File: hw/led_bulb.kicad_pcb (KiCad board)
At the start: 2 copper layers, 92.4 x 91.4 mm, 167 parts, among them P1 USB_OTG, P10 CONN_01X02, P11 CONN_01X02, P12 CONN_01X02, P13 CONN_01X02, P14 CONN_01X02, P15 CONN_01X02, P16 CONN_01X02, P17 CONN_01X02, P18 CONN_01X02, P19 CONN_01X02, P2 CONN_01X02, P20 CONN_01X02, P21 CONN_01X02, P22 CONN_01X02, P23 CONN_01X02, P24 CONN_01X02, P25 CONN_01X02, P26 CONN_01X02, P27 CONN_01X02, P28 CONN_01X02, P29 CONN_01X02, P3 CONN_01X02, P30 CONN_01X02, P31 CONN_01X02, P32 CONN_01X02, P33 CONN_01X02, P4 CONN_01X02, P5 CONN_01X02, P6 CONN_01X02, P7 CONN_01X02, P8 CONN_01X02, P9 CONN_01X02, SW1 SW_RST, SW2 SW_FLASH, U1 CP2102, U3 ESP-12E, U4 AP1117D33

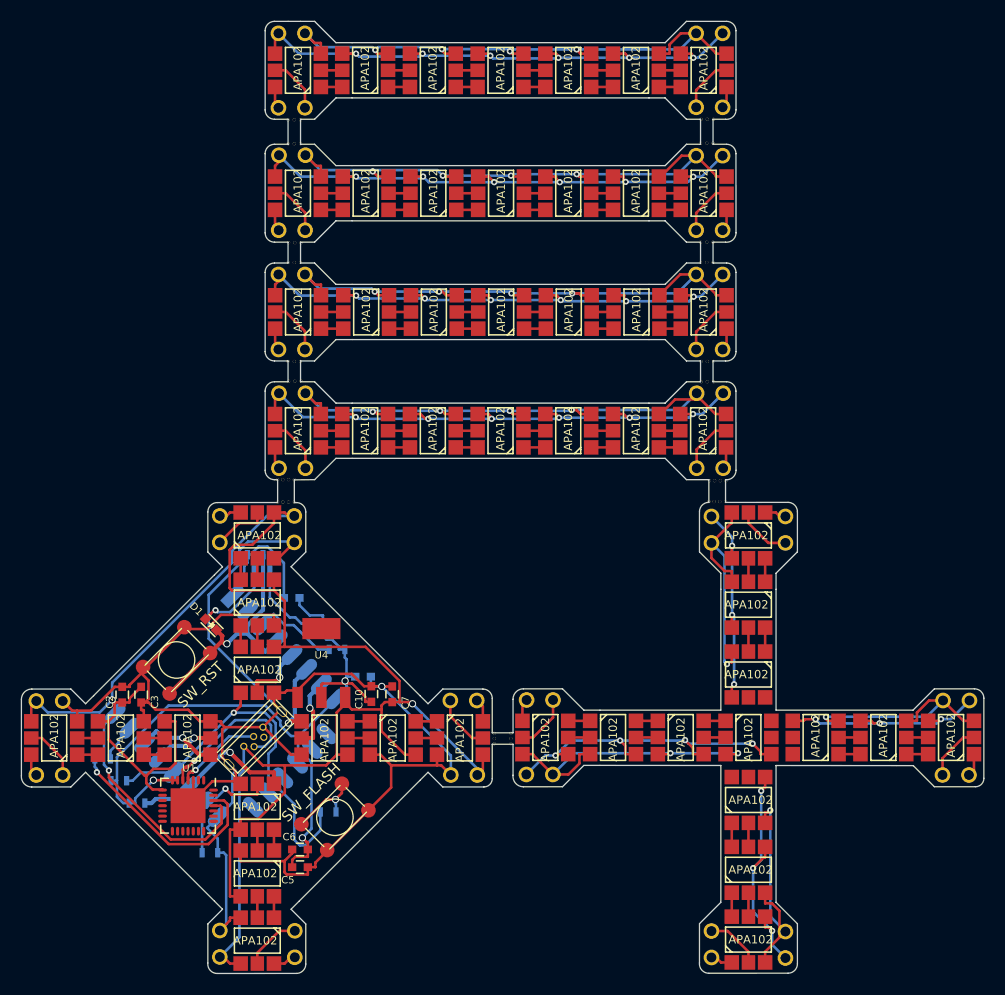
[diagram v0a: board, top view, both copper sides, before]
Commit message: Added transistor to allow automatic flashing.
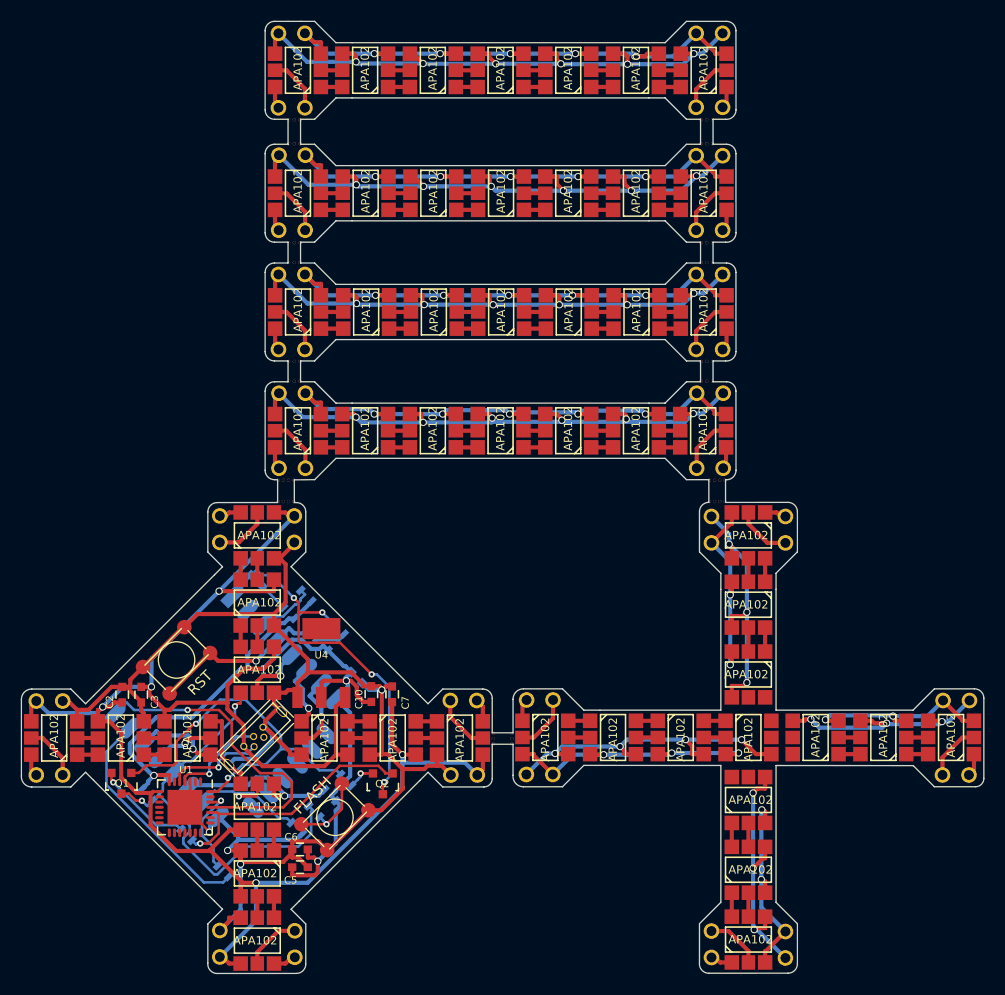
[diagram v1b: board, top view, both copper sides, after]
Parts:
- removed D1: LED_BLUE, LEDs:LED-0603
- removed the HOLE0 at (130.1, 145.7)
- removed the HOLE0 at (109.8, 109.5)
- removed the HOLE0 at (108.7, 109.5)
- removed the HOLE0 at (109.8, 100.0)
- removed the HOLE0 at (108.7, 100.0)
- removed the HOLE0 at (109.9, 98.0)
- removed the HOLE0 at (109.3, 98.0)
- removed the HOLE0 at (109.8, 88.5)
- removed the HOLE0 at (130.1, 145.2)
- removed the HOLE0 at (108.7, 88.5)
- removed the HOLE0 at (109.8, 86.2)
- removed the HOLE0 at (108.7, 86.2)
- removed the HOLE0 at (149.5, 86.2)
- removed the HOLE0 at (148.3, 86.2)
- removed the HOLE0 at (148.9, 86.2)
- removed the HOLE0 at (149.4, 88.5)
- removed the HOLE0 at (148.2, 88.5)
- removed the HOLE0 at (130.1, 146.2)
- removed the HOLE0 at (148.8, 88.5)
- removed the HOLE0 at (149.4, 98.0)
- removed the HOLE0 at (148.2, 98.0)
- removed the HOLE0 at (148.8, 98.0)
- removed the HOLE0 at (149.4, 100.0)
- removed the HOLE0 at (148.2, 100.0)
- removed the HOLE0 at (149.5, 109.5)
- removed the HOLE0 at (148.9, 109.5)
- removed the HOLE0 at (128.4, 145.7)
- removed the HOLE0 at (149.6, 120.9)
- removed the HOLE0 at (150.2, 120.9)
- removed the HOLE0 at (149.1, 120.9)
- removed the HOLE0 at (150.7, 120.9)
- removed the HOLE0 at (149.1, 122.9)
- removed the HOLE0 at (149.6, 122.9)
- removed the HOLE0 at (150.7, 122.9)
- removed the HOLE0 at (108.7, 120.8)
- removed the HOLE0 at (109.2, 120.8)
- removed the HOLE0 at (128.4, 145.2)
- removed the HOLE0 at (108.2, 120.8)
- removed the HOLE0 at (107.7, 120.8)
- removed the HOLE0 at (109.2, 123.0)
- removed the HOLE0 at (108.7, 123.0)
- removed the HOLE0 at (108.2, 123.0)
- removed the HOLE0 at (107.7, 123.0)
- removed the HOLE0 at (149.5, 111.4)
- removed the HOLE0 at (148.9, 111.4)
- removed the HOLE0 at (148.3, 111.4)
- removed the HOLE0 at (128.4, 146.2)
- removed the HOLE0 at (109.9, 111.3)
- removed the HOLE0 at (109.3, 111.3)
- added HOLE0: 0.3mm, footprints:0.3mm, F.Cu at (128.3, 146.2)
- added HOLE0: 0.3mm, footprints:0.3mm, F.Cu at (148.8, 109.5)
- added HOLE0: 0.3mm, footprints:0.3mm, F.Cu at (149.4, 109.5)
- added HOLE0: 0.3mm, footprints:0.3mm, F.Cu at (148.3, 100.0)
- added HOLE0: 0.3mm, footprints:0.3mm, F.Cu at (149.4, 100.0)
- added HOLE0: 0.3mm, footprints:0.3mm, F.Cu at (148.3, 98.0)
- added HOLE0: 0.3mm, footprints:0.3mm, F.Cu at (148.8, 98.0)
- added HOLE0: 0.3mm, footprints:0.3mm, F.Cu at (149.4, 98.0)
- added HOLE0: 0.3mm, footprints:0.3mm, F.Cu at (148.3, 88.5)
- added HOLE0: 0.3mm, footprints:0.3mm, F.Cu at (128.3, 145.7)
- added HOLE0: 0.3mm, footprints:0.3mm, F.Cu at (148.8, 88.5)
- added HOLE0: 0.3mm, footprints:0.3mm, F.Cu at (149.4, 88.5)
- added HOLE0: 0.3mm, footprints:0.3mm, F.Cu at (148.3, 86.2)
- added HOLE0: 0.3mm, footprints:0.3mm, F.Cu at (148.8, 86.2)
- added HOLE0: 0.3mm, footprints:0.3mm, F.Cu at (149.4, 86.2)
- added HOLE0: 0.3mm, footprints:0.3mm, F.Cu at (108.7, 86.2)
- added HOLE0: 0.3mm, footprints:0.3mm, F.Cu at (109.8, 86.2)
- added HOLE0: 0.3mm, footprints:0.3mm, F.Cu at (108.7, 88.5)
- added HOLE0: 0.3mm, footprints:0.3mm, F.Cu at (128.3, 145.2)
- added HOLE0: 0.3mm, footprints:0.3mm, F.Cu at (109.8, 88.5)
- added HOLE0: 0.3mm, footprints:0.3mm, F.Cu at (109.8, 98.0)
- added HOLE0: 0.3mm, footprints:0.3mm, F.Cu at (109.2, 98.0)
- added HOLE0: 0.3mm, footprints:0.3mm, F.Cu at (109.8, 100.0)
- added HOLE0: 0.3mm, footprints:0.3mm, F.Cu at (108.7, 100.0)
- added HOLE0: 0.3mm, footprints:0.3mm, F.Cu at (109.8, 109.5)
- added HOLE0: 0.3mm, footprints:0.3mm, F.Cu at (108.7, 109.5)
- added HOLE0: 0.3mm, footprints:0.3mm, F.Cu at (130.2, 146.2)
- added HOLE0: 0.3mm, footprints:0.3mm, F.Cu at (109.8, 111.3)
- added HOLE0: 0.3mm, footprints:0.3mm, F.Cu at (109.2, 111.3)
- added HOLE0: 0.3mm, footprints:0.3mm, F.Cu at (109.2, 122.9)
- added HOLE0: 0.3mm, footprints:0.3mm, F.Cu at (108.7, 122.9)
- added HOLE0: 0.3mm, footprints:0.3mm, F.Cu at (108.2, 122.9)
- added HOLE0: 0.3mm, footprints:0.3mm, F.Cu at (107.7, 122.9)
- added HOLE0: 0.3mm, footprints:0.3mm, F.Cu at (150.6, 122.9)
- added HOLE0: 0.3mm, footprints:0.3mm, F.Cu at (149.6, 122.9)
- added HOLE0: 0.3mm, footprints:0.3mm, F.Cu at (130.2, 145.7)
- added HOLE0: 0.3mm, footprints:0.3mm, F.Cu at (149.1, 122.9)
- added HOLE0: 0.3mm, footprints:0.3mm, F.Cu at (150.6, 120.8)
- added HOLE0: 0.3mm, footprints:0.3mm, F.Cu at (150.1, 120.8)
- added HOLE0: 0.3mm, footprints:0.3mm, F.Cu at (149.6, 120.8)
- added HOLE0: 0.3mm, footprints:0.3mm, F.Cu at (149.1, 120.8)
- added HOLE0: 0.3mm, footprints:0.3mm, F.Cu at (107.7, 120.8)
- added HOLE0: 0.3mm, footprints:0.3mm, F.Cu at (108.2, 120.8)
- added HOLE0: 0.3mm, footprints:0.3mm, F.Cu at (109.2, 120.8)
- added HOLE0: 0.3mm, footprints:0.3mm, F.Cu at (108.7, 120.8)
- added HOLE0: 0.3mm, footprints:0.3mm, F.Cu at (130.2, 145.2)
- added HOLE0: 0.3mm, footprints:0.3mm, F.Cu at (148.3, 111.3)
- added HOLE0: 0.3mm, footprints:0.3mm, F.Cu at (148.8, 111.3)
- added HOLE0: 0.3mm, footprints:0.3mm, F.Cu at (149.4, 111.3)
- added Q1: Q_NPN_EBC, TO_SOT_Packages_SMD:SOT-23, F.Cu at (92.7, 149.9)
- added Q2: Q_NPN_EBC, TO_SOT_Packages_SMD:SOT-23, F.Cu at (117.8, 150.0)
- added R10: 470, Resistors_SMD:R_0603, B.Cu at (111.2, 152.7)
- added R11: 470, Resistors_SMD:R_0603, B.Cu at (102.4, 158.4)
- R6, R7, R8: value 470 -> 12k
- SW1: value SW_RST -> RST
- SW2: value SW_FLASH -> FLASH
- moved R6 26.5 mm to (98.9, 154.9), turned to 135 degrees
- moved R8 23.8 mm to (112.0, 136.7), turned to 135 degrees
- moved R7 23.3 mm to (114.2, 149.6), turned to 315 degrees
- moved R2 18.6 mm to (112.7, 151.1), turned to 315 degrees
- moved R9 17.6 mm to (113.5, 135.1), turned to 315 degrees
- moved R5 8.68 mm to (109.5, 154.2), turned to 315 degrees
- moved R3 5.94 mm to (110.4, 131.9), turned to 315 degrees
- moved C4 3.73 mm to (105.7, 130.5), turned to 315 degrees
- moved R1 3.06 mm to (95.2, 151.1), turned to 135 degrees
- moved R4 2.69 mm to (108.8, 133.6), turned to 315 degrees
- moved C8 0.61 mm to (115.2, 139.8), turned to 315 degrees
- moved U1 0.34 mm to (98.8, 152.2)
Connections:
- R6 pad 1: V_3.3 -> RTS
- R7 pad 1: nRST -> DTR
- R7 pad 2: GPIO16 -> Net-(Q2-Pad2)
- R8 pad 1: Net-(R8-Pad1) -> V_3.3
- R8 pad 2: RX -> GPIO16
- R9 pad 1: GPIO0 -> nRST
- R9 pad 2: Net-(R9-Pad2) -> GPIO16
- SW2 pad 1: Net-(R9-Pad2) -> Net-(R10-Pad2)
- U1 pad 24: Net-(U1-Pad24) -> RTS
- U1 pad 26: Net-(R8-Pad1) -> Net-(R11-Pad1)
- U1 pad 28: Net-(U1-Pad28) -> DTR
- U1 pad 6: V_3.3 -> Net-(U1-Pad6)
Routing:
- net DTR: track 0.00 -> 36.6 mm, vias 0 -> 2
- net RTS: track 0.00 -> 24.9 mm, vias 0 -> 1
- net nRST: track 12.5 -> 37.2 mm, vias 0 -> 4
- net GND: track 185.3 -> 161.1 mm, vias 1 -> 4
- net Net-(R8-Pad1): track 21.0 -> 0.00 mm, vias 1 -> 0
- net RX: track 3.71 -> 22.2 mm
- net V_USB: track 183.0 -> 171.0 mm, vias 2 -> 5
- net Net-(R11-Pad1): track 0.00 -> 8.68 mm, vias 0 -> 1
- net TX: track 23.1 -> 31.6 mm
- net Net-(R10-Pad2): track 0.00 -> 7.89 mm, vias 0 -> 1
- net Net-(R9-Pad2): track 7.25 -> 0.00 mm, vias 1 -> 0
- net USB_D-: track 15.2 -> 9.36 mm
- net GPIO0: track 37.3 -> 42.2 mm, vias 1 -> 2
- net Net-(LED14-Pad4): track 55.9 -> 60.3 mm
- net Net-(LED14-Pad3): track 56.4 -> 52.6 mm, vias 4 -> 5
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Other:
- net class Power: trace_width 0.25 -> 0.4

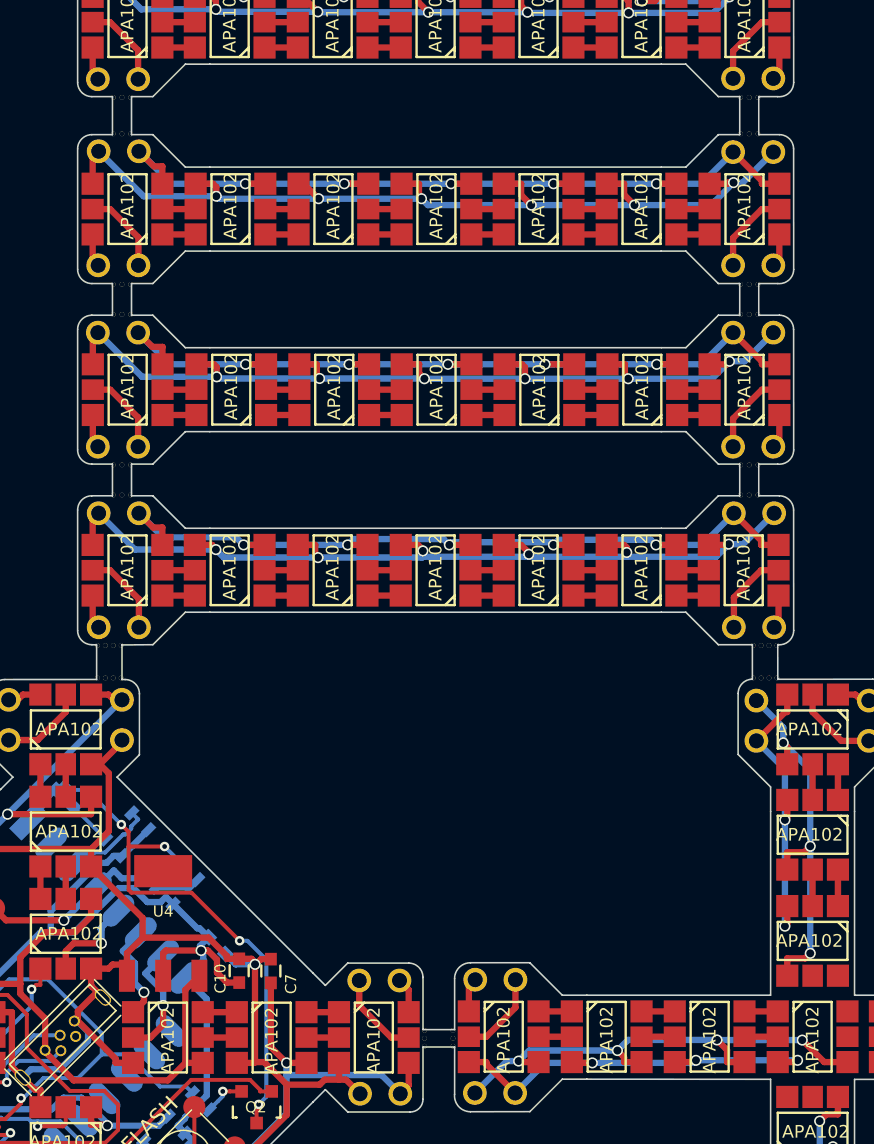
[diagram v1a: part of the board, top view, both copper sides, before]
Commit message: Switched to non-plated holes for mouse bites.
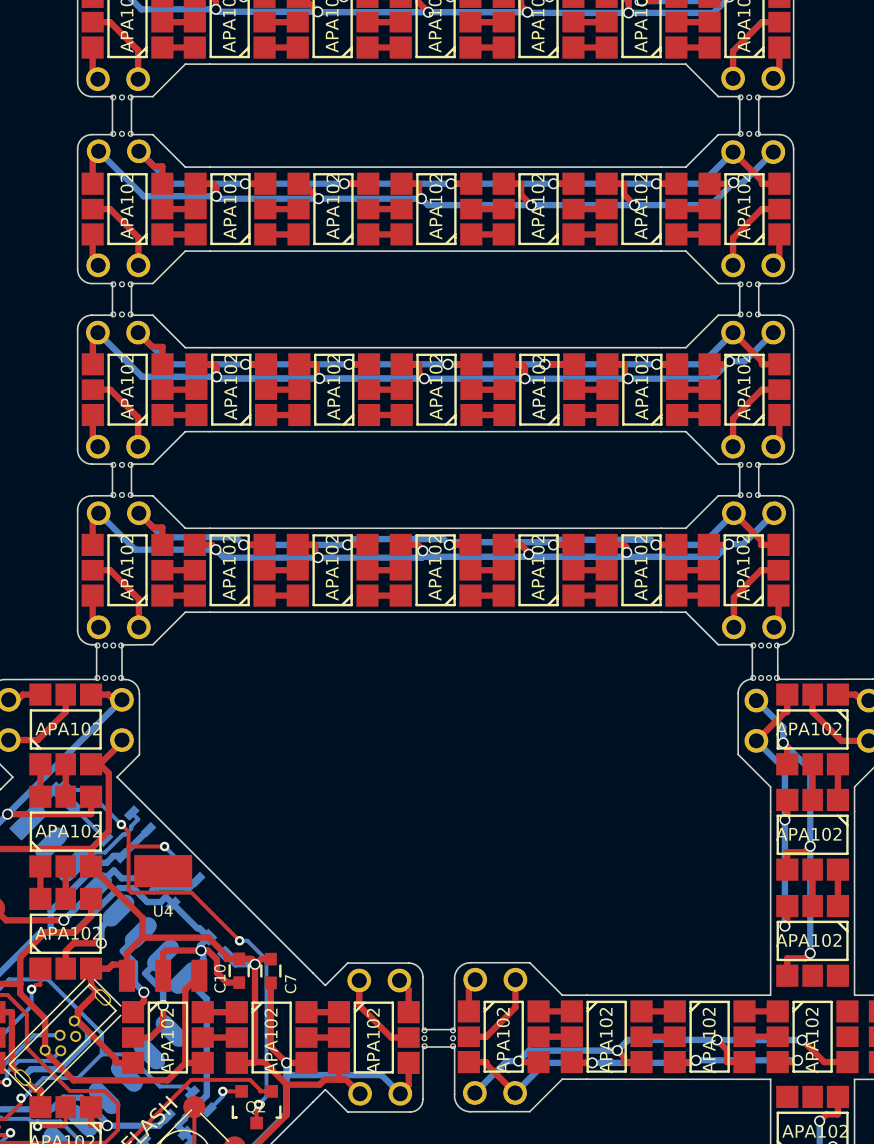
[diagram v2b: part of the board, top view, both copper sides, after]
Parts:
- HOLE0 (x58): footprint footprints:0.3mm -> footprints:hole_0.3mm
